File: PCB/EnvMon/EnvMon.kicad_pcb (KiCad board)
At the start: 2 copper layers, 44.5 x 37 mm, 33 parts, among them J1 USB-C, J2 DC, J3 GPIO, M1 SCD30-4pin, M2 OLED1.5-RGB, U1 LMR16006+FB, U2 FT231XQ, U3 ESP32-WROOM-32

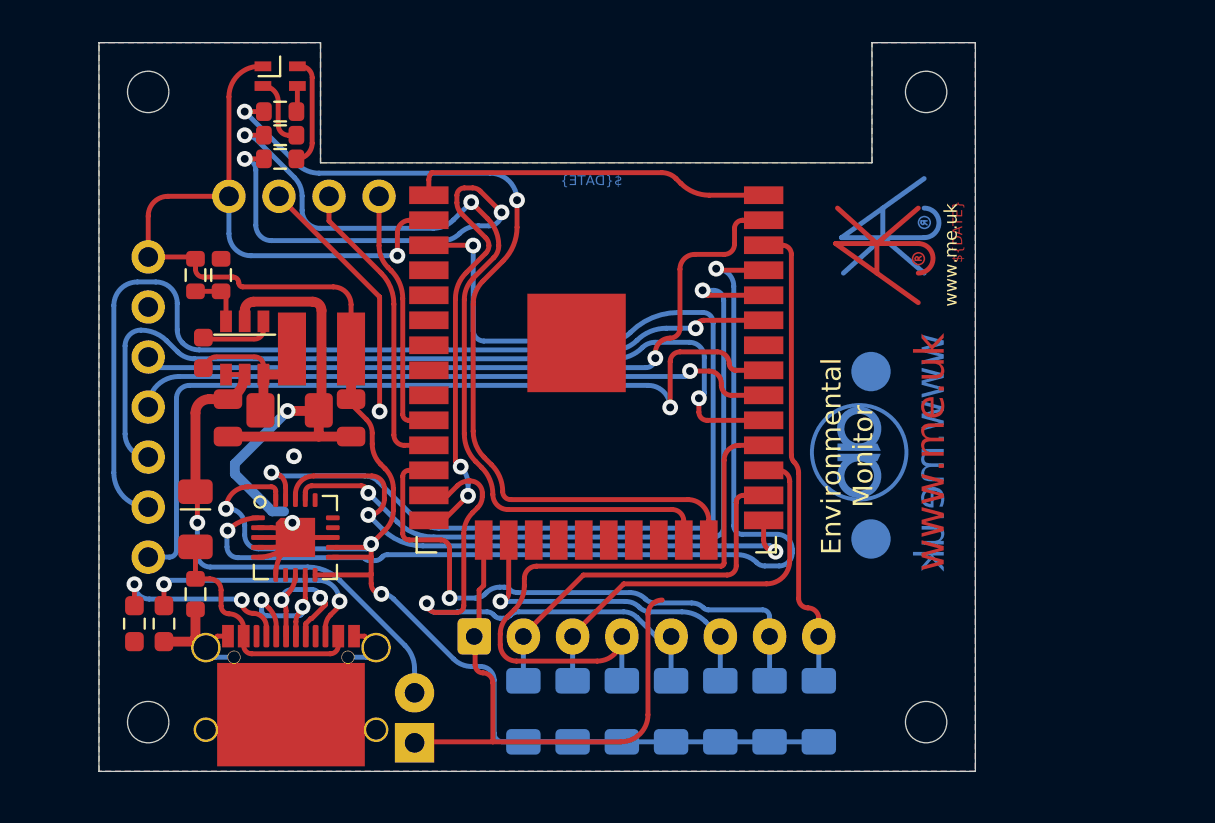
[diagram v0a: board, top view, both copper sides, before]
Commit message: S3 board basic tracking started
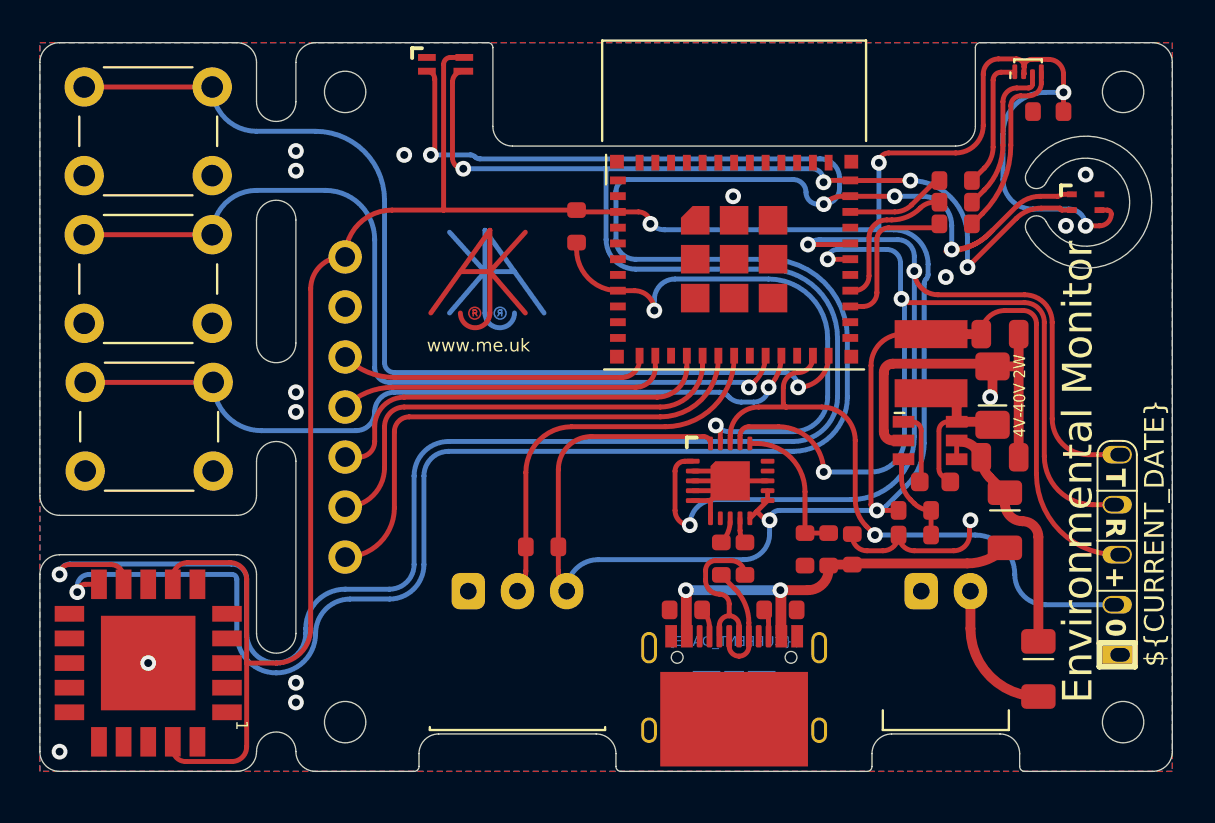
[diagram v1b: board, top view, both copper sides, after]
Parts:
- removed Logo3: AJK, RevK:AJK
- removed M2: OLED1.5-RGB, RevK:OLED1.5-RGB
- removed R14: NF, Resistor_SMD:R_1206_3216Metric_Pad1.30x1.75mm_HandSolder
- added C5: 100nF, RevK:C_0603, F.Cu at (138.2, 66.5)
- added D4: D, RevK:D_1206, F.Cu at (137.7, 94.8)
- added J4: Shelly, RevK:Shelly, F.Cu at (141.7, 89.0)
- added SW1: SW_Push, Button_Switch_THT:SW_PUSH_6mm_H13mm, F.Cu at (89.2, 65.2)
- added SW2: SW_Push, Button_Switch_THT:SW_PUSH_6mm_H13mm, F.Cu at (89.2, 72.8)
- added SW3: SW_Push, Button_Switch_THT:SW_PUSH_6mm_H13mm, F.Cu at (89.3, 80.2)
- added U4: ESP32-PICO-MINI-02, RevK:ESP32-PICO-MINI-02, F.Cu at (122.2, 74.0)
- added U5: QR, RevK:QR-ENVMON, B.Cu at (122.2, 97.0)
- added U7: SHT40, RevK:Sensirion_DFN-4_1.5x1.5mm_P0.5mm_SHT4x, F.Cu at (140.1, 71.1)
- added U8: VEML6040, RevK:VEML6040, F.Cu at (107.6, 64.1)
- C1: value 0.1uF -> 100nF; footprint RevK:Hidden -> RevK:C_0603_
- C2, C3: footprint RevK:Hidden -> RevK:C_0805_
- D1: footprint RevK:Hidden -> RevK:D_1206_
- D3: value RGB -> LED_BARG; footprint RevK:LED-RGB-1.6x1.6 -> RevK:MHS190RGBCT
- J1: footprint RevK:USC16-TR-Round -> RevK:USC16-TR
- J2: footprint RevK:DC -> RevK:PTSM-HH-2-RA-W; moved to F.Cu
- J3: value GPIO -> TEMP; footprint RevK:Molex_MiniSPOX_H8RA -> RevK:PTSM-HH-3-RA
- L1: footprint RevK:Hidden -> RevK:L_4x4_
- Logo1: value AA -> AJK; footprint RevK:AA -> RevK:AJK
- Logo2: moved to F.Cu
- M1: value SCD30-4pin -> OLED1.5-RGB; footprint RevK:SCD30-4pin -> RevK:OLED1.5-RGB; moved to F.Cu
- R1: value 100k 1% or 0R -> 100k 1%
- R10, R13: value NF -> 4k7; footprint Resistor_SMD:R_1206_3216Metric_Pad1.30x1.75mm_HandSolder -> RevK:R_0603; moved to F.Cu
- R11, R12: value NF -> 10k; footprint Resistor_SMD:R_1206_3216Metric_Pad1.30x1.75mm_HandSolder -> RevK:R_0603; moved to F.Cu
- R2: value 30k 1% or NF -> 30k 1%
- R3, R4: footprint Resistor_SMD:R_0603_1608Metric_Pad0.98x0.95mm_HandSolder -> RevK:R_0603
- R5: value 732R -> 27R
- R6: value 2K -> 27R
- R7: value 324R -> 300R
- R8: value NF -> 1K; footprint Resistor_SMD:R_1206_3216Metric_Pad1.30x1.75mm_HandSolder -> RevK:R_0603; moved to F.Cu
- R9: value NF -> 100R; footprint Resistor_SMD:R_1206_3216Metric_Pad1.30x1.75mm_HandSolder -> RevK:R_0603; moved to F.Cu
- U1: value LMR16006+FB -> LMR16006XDDCR; footprint RevK:RegulatorBlockFB -> RevK:SOT-23-Thin-6-Reg
- U2: value FT231XQ -> SCD41; footprint RevK:QFN-20-1EP_4x4mm_P0.5mm_EP2.5x2.5mm -> RevK:SCD41
- U3: value ESP32-WROOM-32 -> FT231XQ; footprint RevK:ESP32-WROOM-32 -> RevK:QFN-20-1EP_4x4mm_P0.5mm_EP2.5x2.5mm
- moved D2 41.1 mm to (136.0, 87.2)
- moved C2 39.3 mm to (135.8, 84.0), turned to 0 degrees
- moved R1 38.4 mm to (131.4, 86.8), turned to 0 degrees
- moved D3 38.0 mm to (137.2, 64.6), turned to 0 degrees
- moved C1 37.7 mm to (132.4, 85.3), turned to 0 degrees
- moved R2 37.6 mm to (131.4, 88.0), turned to 0 degrees
- moved D1 35.7 mm to (135.4, 80.9), turned to 90 degrees
- moved U1 35.1 mm to (132.2, 83.2), turned to 90 degrees
- moved R7 34.5 mm to (133.5, 71.1)
- moved C4 33.4 mm to (128.2, 88.7), turned to -90 degrees
- moved R9 33.2 mm to (133.5, 70.0), turned to 180 degrees
- moved C3 33.2 mm to (135.8, 77.8), turned to 0 degrees
- moved R8 33.1 mm to (133.5, 72.2), turned to 180 degrees
- moved R4 32.8 mm to (124.6, 91.8), turned to 0 degrees
- moved R6 31.9 mm to (121.6, 89.2), turned to 90 degrees
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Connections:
- D3 pad 1: +3V3 -> Net-(D3-BK)
- D3 pad 2: Net-(D3-Pad2) -> +3.3V
- D3 pad 3: Net-(D3-Pad3) -> Net-(D3-RK)
- D3 pad 4: Net-(D3-Pad4) -> Net-(D3-GK)
- J1 pad A5: Net-(J1-PadA5) -> Net-(J1-CC1)
- J1 pad A6: Net-(J1-PadA6) -> Net-(J1-D+-PadA6)
- J1 pad A7: Net-(J1-PadA7) -> Net-(J1-D--PadA7)
- J1 pad B5: Net-(J1-PadB5) -> Net-(J1-CC2)
- J1 pad B6: Net-(J1-PadA6) -> Net-(J1-D+-PadA6)
- J1 pad B7: Net-(J1-PadA7) -> Net-(J1-D--PadA7)
- J2 pad 2: DC -> Net-(D4-A)
- J3 pad 2: IO1 -> TEMP
- J3 pad 3: IO2 -> +3.3V
- M1 pad 1: +3V3 -> +3.3V
- M1 pad 3: CO2-SCL -> OLED-MOSI
- M1 pad 4: CO2-SDA -> OLED-SCK
- R1 pad 1: +3V3 -> +3.3V
- R1 pad 2: Net-(R1-Pad2) -> Net-(U1-FB)
- R10 pad 1: IO3 -> VBUS
- R10 pad 2: +3V3 -> Net-(U3-CBUS3)
- R11 pad 1: IO4 -> Net-(U3-CBUS3)
- R11 pad 2: +3V3 -> GND
- R12 pad 1: IO5 -> +3.3V
- R12 pad 2: +3V3 -> EN
- R13 pad 1: IO6 -> TEMP
- R13 pad 2: +3V3 -> +3.3V
- R2 pad 2: Net-(R1-Pad2) -> Net-(U1-FB)
- R3 pad 1: Net-(J1-PadB5) -> Net-(J1-CC1)
- R4 pad 1: Net-(J1-PadA5) -> Net-(J1-CC2)
- R5 pad 1: Net-(D3-Pad2) -> Net-(J1-D--PadA7)
- R5 pad 2: R -> D-
- R6 pad 1: Net-(D3-Pad3) -> Net-(J1-D+-PadA6)
- R6 pad 2: G -> D+
- R7 pad 1: Net-(D3-Pad4) -> Net-(D3-RK)
- R7 pad 2: B -> R
- R8 pad 1: IO1 -> Net-(D3-GK)
- R8 pad 2: +3V3 -> G
- R9 pad 1: IO2 -> Net-(D3-BK)
- R9 pad 2: +3V3 -> B
- U1 pad 1: DC -> unconnected-(U1-CB-Pad1)
- U1 pad 2: DC -> GND
- U1 pad 3: GND -> Net-(U1-FB)
- U1 pad 4: +3V3 -> DC
- U1 pad 5: Net-(R1-Pad2) -> DC
- U2 pad 1: Net-(U2-Pad1) -> unconnected-(U2-DNC-Pad1)
- U2 pad 10: +3V3 -> SDA
- U2 pad 11: +3V3 -> unconnected-(U2-DNC-Pad11)
- U2 pad 12: +3V3 -> unconnected-(U2-DNC-Pad12)
- U2 pad 13: GND -> unconnected-(U2-DNC-Pad13)
- U2 pad 17: Net-(U2-Pad17) -> unconnected-(U2-DNC-Pad17)
- U2 pad 18: Net-(U2-Pad18) -> unconnected-(U2-DNC-Pad18)
- U2 pad 19: Net-(U2-Pad19) -> +3.3V
- U2 pad 2: GND -> unconnected-(U2-DNC-Pad2)
- U2 pad 20: +3V3 -> GND
- U2 pad 3: GND -> unconnected-(U2-DNC-Pad3)
- U2 pad 4: GND -> unconnected-(U2-DNC-Pad4)
- U2 pad 5: GND -> unconnected-(U2-DNC-Pad5)
- U2 pad 7: unconnected-(U2-Pad7) -> +3.3V
- U2 pad 8: Net-(J1-PadA6) -> unconnected-(U2-DNC-Pad8)
- U2 pad 9: Net-(J1-PadA7) -> SCL
- U3 pad 1: GND -> O
- U3 pad 10: CO2-SDA -> +3.3V
- U3 pad 11: CO2-SCL -> +3.3V
- U3 pad 12: IO6 -> +3.3V
- U3 pad 13: IO4 -> GND
- U3 pad 14: R -> unconnected-(U3-CBUS1-Pad14)
- U3 pad 15: GND -> unconnected-(U3-CBUS0-Pad15)
- U3 pad 16: IO5 -> Net-(U3-CBUS3)
- U3 pad 17: unconnected-(U3-Pad17) -> I
- U3 pad 18: unconnected-(U3-Pad18) -> BOOT
- U3 pad 19: unconnected-(U3-Pad19) -> EN
- U3 pad 2: +3V3 -> GND
- U3 pad 20: unconnected-(U3-Pad20) -> +3.3V
- U3 pad 21: unconnected-(U3-Pad21) -> GND
- U3 pad 3: Net-(U2-Pad19) -> GND
- U3 pad 4: unconnected-(U3-Pad4) -> GND
- U3 pad 5: unconnected-(U3-Pad5) -> GND
- U3 pad 6: unconnected-(U3-Pad6) -> GND
- U3 pad 8: unconnected-(U3-Pad8) -> D+
- U3 pad 9: unconnected-(U3-Pad9) -> D-
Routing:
- net +3.3V: track 0.00 -> 194.9 mm, vias 0 -> 6
- net SDA: track 0.00 -> 131.8 mm, vias 0 -> 5
- net SCL: track 0.00 -> 119.1 mm, vias 0 -> 5
- net +3V3: track 99.7 -> 0.00 mm, vias 4 -> 0
- net GND: track 91.7 -> 19.8 mm, vias 4 -> 15
- net Net-(U2-Pad19): track 55.2 -> 0.00 mm, vias 2 -> 0
- net O: track 0.00 -> 52.8 mm, vias 0 -> 3
- net Net-(U2-Pad1): track 51.9 -> 0.00 mm, vias 2 -> 0
- net BUTTON1: track 0.00 -> 50.6 mm, vias 0 -> 1
- net I: track 0.00 -> 45.2 mm, vias 0 -> 3
- net BUTTON2: track 0.00 -> 45.2 mm, vias 0 -> 1
- net OLED-CS0: track 43.6 -> 0.00 mm, vias 1 -> 0
- net BUTTON3: track 0.00 -> 39.3 mm, vias 0 -> 1
- net Net-(U2-Pad17): track 39.2 -> 0.00 mm, vias 2 -> 0
- net B: track 43.4 -> 5.11 mm, vias 2 -> 0
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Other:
- board size 44.5 x 37 mm -> 57.5 x 37 mm
- board text added: "${CURRENT_DATE}"
- board text added: "13"
- board text added: "14"
- board text added: "15"
- board text added: "25"
- board text added: "26"
- board text added: "27"
- board text added: "3.3"
- board text added: "32"
- board text added: "33"
- board text added: "4"
- board text added: "CLK"
- board text added: "CO₂"
- board text added: "CS"
- board text added: "DC"
- board text added: "DC 4V-40V 2W"
- board text added: "DIN"
- board text added: "DS18B20"
- board text added: "RST"
- board text added: "SCD41"
- board text added: "SCL: 21 SDA: 22 RGB: 8/7/19"
- board text added: "SHT40"
- board text added: "VEML6040"
- board text added: "⏚"
- board text removed: "${DATE}"
- board text removed: "www.me.uk"

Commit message: One board
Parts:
- removed C4: 10nF, RevK:C_0603
- removed D4: D, RevK:D_1206
- removed J4: Shelly, RevK:Shelly
- removed L1: 6.8uH, RevK:L_4x4_
- removed R10: 4k7, RevK:R_0603
- removed R11, R12: 10k, RevK:R_0603
- removed R6: 27R, RevK:R_0603
- removed R7: 300R, RevK:R_0603
- removed R8: 1K, RevK:R_0603
- removed R9: 100R, RevK:R_0603
- removed U3: FT231XQ, RevK:QFN-20-1EP_4x4mm_P0.5mm_EP2.5x2.5mm
- removed U4: ESP32-PICO-MINI-02, RevK:ESP32-PICO-MINI-02
- added C6: 10uF 50V, RevK:C_0603_, F.Cu at (131.7, 83.2)
- added C7: 10uF 6.3V, RevK:C_0603_, F.Cu at (136.7, 83.2)
- added C8: 100nF, RevK:C_0603_, F.Cu at (134.2, 83.9)
- added J5: Shelly, RevK:Shelly, B.Cu at (122.2, 81.1)
- added L2: 10uH, RevK:L_4x4_, F.Cu at (134.2, 86.5)
- added R14: 124k, RevK:R_0402_, F.Cu at (134.2, 80.0)
- added R15: 39k2, RevK:R_0402_, F.Cu at (136.7, 81.1)
- added R16: 1M, RevK:R_0402_, F.Cu at (131.7, 81.1)
- added R17: 220R, RevK:R_0402, F.Cu at (135.7, 66.3)
- added U6: MD8942, RevK:SOT-23-6-MD8942, F.Cu at (134.2, 81.9)
- C1: footprint RevK:C_0603_ -> RevK:C_0402
- C2: value 2.2uF -> 22uF; footprint RevK:C_0805_ -> RevK:C_0402
- C3: value 10uF -> 1uF; footprint RevK:C_0805_ -> RevK:C_0402
- C5: footprint RevK:C_0603 -> RevK:C_0402
- D1: value Schottky -> RGB; footprint RevK:D_1206_ -> RevK:LED-RGB-1.6x1.6
- D2: footprint RevK:D_1206 -> RevK:D_SOD-123
- D3: value LED_BARG -> D; footprint RevK:MHS190RGBCT -> RevK:D_SOD-123
- R1: value 100k 1% -> 680R; footprint RevK:R_0603 -> RevK:R_0402
- R13, R3, R4: footprint RevK:R_0603 -> RevK:R_0402
- R2: value 30k 1% -> 2K; footprint RevK:R_0603 -> RevK:R_0402
- R5: value 27R -> 10K; footprint RevK:R_0603 -> RevK:R_0402
- U1: value LMR16006XDDCR -> ESP32-S3-MINI-1; footprint RevK:SOT-23-Thin-6-Reg -> RevK:ESP32-S3-MINI-1
- moved D3 27.8 mm to (126.5, 90.3), turned to -90 degrees
- moved C2 26.0 mm to (113.0, 71.3), turned to 90 degrees
- moved C1 23.3 mm to (113.8, 71.3), turned to 90 degrees
- moved R2 22.4 mm to (137.2, 66.3), turned to -90 degrees
- moved R1 21.0 mm to (136.4, 66.3), turned to -90 degrees
- moved R5 20.2 mm to (130.7, 70.6)
- moved D1 16.5 mm to (136.4, 64.5), turned to 180 degrees
- moved U1 12.3 mm to (122.2, 76.0), turned to 0 degrees
- moved C3 8.39 mm to (131.4, 70.6), turned to -90 degrees
- moved D2 8.14 mm to (128.4, 90.3)
- moved Logo1 6.30 mm to (111.3, 80.7)
- moved C5 3.76 mm to (140.6, 69.4)
- moved Logo2 1.77 mm to (108.5, 75.7), turned to -90 degrees
- moved R3 1.03 mm to (120.5, 91.0)
- moved R4 0.87 mm to (124.2, 91.0)
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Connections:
- D2 pad 2: VBUS -> Net-(D2-A)
- D3 pad 1: Net-(D3-BK) -> DC
- D3 pad 2: +3.3V -> Net-(D3-A)
- J1 pad A4: VBUS -> Net-(D3-A)
- J1 pad A6: Net-(J1-D+-PadA6) -> D+
- J1 pad A7: Net-(J1-D--PadA7) -> D-
- J1 pad A9: VBUS -> Net-(D3-A)
- J1 pad B4: VBUS -> Net-(D3-A)
- J1 pad B6: Net-(J1-D+-PadA6) -> D+
- J1 pad B7: Net-(J1-D--PadA7) -> D-
- J1 pad B9: VBUS -> Net-(D3-A)
- J2 pad 2: Net-(D4-A) -> Net-(D2-A)
- R1 pad 1: +3.3V -> Net-(D1-RK)
- R1 pad 2: Net-(U1-FB) -> R
- R2 pad 1: GND -> Net-(D1-GK)
- R2 pad 2: Net-(U1-FB) -> G
- R5 pad 1: Net-(J1-D--PadA7) -> +3.3V
- R5 pad 2: D- -> Net-(U1-EN)
- U1 pad 1: unconnected-(U1-CB-Pad1) -> GND
- U1 pad 3: Net-(U1-FB) -> +3.3V
- U1 pad 4: DC -> Net-(J5-0)
- U1 pad 5: DC -> unconnected-(U1-GPIO1-Pad5)
- U1 pad 7: +3.3V -> unconnected-(U1-GPIO3-Pad7)
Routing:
- net O: track 52.8 -> 0.00 mm, vias 3 -> 0
- net I: track 45.2 -> 0.00 mm, vias 3 -> 0
- net +3.3V: track 194.9 -> 154.4 mm, vias 6 -> 3
- net SDA: track 131.8 -> 95.7 mm, vias 5 -> 3
- net BOOT: track 31.1 -> 0.00 mm, vias 1 -> 0
- net EN: track 28.1 -> 0.00 mm, vias 2 -> 0
- net VBUS: track 26.2 -> 0.00 mm, vias 2 -> 0
- net SCL: track 119.1 -> 95.0 mm, vias 5 -> 3
- net BUTTON1: track 50.6 -> 29.9 mm, vias 1 -> 0
- net GND: track 19.8 -> 2.72 mm, vias 15 -> 17
- net BUTTON2: track 45.2 -> 29.9 mm, vias 1 -> 0
- net Net-(J5-0): track 0.00 -> 12.4 mm
- net D+: track 1.20 -> 12.8 mm
- net D-: track 1.29 -> 12.7 mm
- net OLED-RST: track 26.1 -> 15.1 mm
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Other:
- outline, holes or cut-outs redrawn
- board text added: "10"
- board text added: "11"
- board text added: "12"
- board text added: "5"
- board text added: "6"
- board text added: "7"
- board text added: "8"
- board text added: "9"
- board text added: "DC 4V-36V"
- board text added: "SCL: 38 SDA: 39 RGB: 41/40/42"
- board text removed: "13"
- board text removed: "14"
- board text removed: "15"
- board text removed: "25"
- board text removed: "26"
- board text removed: "27"
- board text removed: "32"
- board text removed: "33"
- board text removed: "DC 4V-40V 2W"
- board text removed: "SCL: 21 SDA: 22 RGB: 8/7/19"

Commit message: New reg
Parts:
- moved R15 1.30 mm to (135.9, 80.0), turned to 0 degrees
- moved R16 1.30 mm to (132.3, 80.0), turned to 0 degrees

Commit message: Tidy
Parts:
- moved Logo2 14.4 mm to (118.2, 86.2), turned to 0 degrees
- moved R15 0.59 mm to (136.1, 80.6)
- moved C6 0.59 mm to (131.8, 83.8)
- moved C7 0.59 mm to (136.8, 83.8)
- moved C8 0.59 mm to (134.2, 84.5)
- moved L2 0.59 mm to (134.2, 87.1)
- moved R14 0.59 mm to (134.2, 80.6)
- moved R16 0.59 mm to (132.4, 80.6)
- moved U6 0.59 mm to (134.2, 82.5)
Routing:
- net Net-(D2-A): track 6.57 -> 8.52 mm
- net +3.3V: track 154.4 -> 155.4 mm
- net GND: vias 17 -> 20
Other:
- board text added: "RGB: 41/40/42"
- board text added: "SCL: 38 SDA: 39"
- board text removed: "SCL: 38 SDA: 39 RGB: 41/40/42"
